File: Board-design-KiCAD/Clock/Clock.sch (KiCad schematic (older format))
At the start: 19 parts, among them M1 SevSeg4Inch, M2 SevSeg4Inch, Y1 SevSeg1.8Inch, Y2 SevSeg1.8Inch, Y3 SevSeg1.8Inch, Y4 SevSeg1.8Inch

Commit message: Add some components
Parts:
- removed U? (x4): ULN2003A, symbol Transistor_Array:ULN2003A
- added U? (x3): 74HC595, symbol 74xx:74HC595
- added U? (x2): ULN2003A, symbol Transistor_Array:ULN2003A
- added U? (x7): 74HC14, symbol 74xx:74HC14
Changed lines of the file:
@@
-$EndComp
-$Comp
-L Transistor_Array:ULN2003A U?
-U 1 1 5F3B85A2
-P 4450 3800
-F 0 "U?" H 4450 4467 50  0000 C CNN
-F 1 "ULN2003A" H 4450 4376 50  0000 C CNN
-F 2 "" H 4500 3250 50  0001 L CNN
-F 3 "http://www.ti.com/lit/ds/symlink/uln2003a.pdf" H 4550 3600 50  0001 C CNN
-	1    4450 3800
-	1    0    0    -1
-$EndComp
-$Comp
-L Transistor_Array:ULN2003A U?
-U 1 1 5F3B9616
-P 5550 3750
-F 0 "U?" H 5550 4417 50  0000 C CNN
-F 1 "ULN2003A" H 5550 4326 50  0000 C CNN
-F 2 "" H 5600 3200 50  0001 L CNN
-F 3 "http://www.ti.com/lit/ds/symlink/uln2003a.pdf" H 5650 3550 50  0001 C CNN
-	1    5550 3750
-	1    0    0    -1
-$EndComp
-$Comp
-L Transistor_Array:ULN2003A U?
-U 1 1 5F3BAC84
-P 6750 3750
-F 0 "U?" H 6750 4417 50  0000 C CNN
-F 1 "ULN2003A" H 6750 4326 50  0000 C CNN
-F 2 "" H 6800 3200 50  0001 L CNN
-F 3 "http://www.ti.com/lit/ds/symlink/uln2003a.pdf" H 6850 3550 50  0001 C CNN
-	1    6750 3750
-	1    0    0    -1
-$EndComp
-$Comp
-L Transistor_Array:ULN2003A U?
-U 1 1 5F3BBFEA
-P 7950 3700
-F 0 "U?" H 7950 4367 50  0000 C CNN
-F 1 "ULN2003A" H 7950 4276 50  0000 C CNN
-F 2 "" H 8000 3150 50  0001 L CNN
-F 3 "http://www.ti.com/lit/ds/symlink/uln2003a.pdf" H 8050 3500 50  0001 C CNN
-	1    7950 3700
-	1    0    0    -1
 $EndComp
 $Comp
@@
 	1    0    0    -1
 $EndComp
-$Comp
-L power:GND #PWR?
-U 1 1 5F3CCD46
-P 4450 4550
-F 0 "#PWR?" H 4450 4300 50  0001 C CNN
-F 1 "GND" H 4455 4377 50  0000 C CNN
-F 2 "" H 4450 4550 50  0001 C CNN
-F 3 "" H 4450 4550 50  0001 C CNN
-	1    4450 4550
-	1    0    0    -1
-$EndComp
-$Comp
-L power:GND #PWR?
-U 1 1 5F3CD13E
-P 5550 4550
-F 0 "#PWR?" H 5550 4300 50  0001 C CNN
-F 1 "GND" H 5555 4377 50  0000 C CNN
-F 2 "" H 5550 4550 50  0001 C CNN
-F 3 "" H 5550 4550 50  0001 C CNN
-	1    5550 4550
-	1    0    0    -1
-$EndComp
-$Comp
-L power:GND #PWR?
-U 1 1 5F3CD53D
-P 6750 4500
-F 0 "#PWR?" H 6750 4250 50  0001 C CNN
-F 1 "GND" H 6755 4327 50  0000 C CNN
-F 2 "" H 6750 4500 50  0001 C CNN
-F 3 "" H 6750 4500 50  0001 C CNN
-	1    6750 4500
-	1    0    0    -1
-$EndComp
-$Comp
-L power:GND #PWR?
-U 1 1 5F3CD948
-P 7950 4400
-F 0 "#PWR?" H 7950 4150 50  0001 C CNN
-F 1 "GND" H 7955 4227 50  0000 C CNN
-F 2 "" H 7950 4400 50  0001 C CNN
-F 3 "" H 7950 4400 50  0001 C CNN
-	1    7950 4400
-	1    0    0    -1
-$EndComp
 Wire Wire Line
 	2000 4450 2000 4550
 Wire Wire Line
 	3300 4400 3300 4550
-Wire Wire Line
-	4450 4400 4450 4550
-Wire Wire Line
-	5550 4350 5550 4550
-Wire Wire Line
-	6750 4350 6750 4500
-Wire Wire Line
-	7950 4300 7950 4400
 $Comp
 L Custom:SevSeg1.8Inch Y3
@@
 	1    0    0    -1
 $EndComp
+$Comp
+L 74xx:74HC595 U?
+U 1 1 5F61C67C
+P 4800 3750
+F 0 "U?" H 4800 4531 50  0000 C CNN
+F 1 "74HC595" H 4800 4440 50  0000 C CNN
+F 2 "" H 4800 3750 50  0001 C CNN
+F 3 "http://www.ti.com/lit/ds/symlink/sn74hc595.pdf" H 4800 3750 50  0001 C CNN
+	1    4800 3750
+	1    0    0    -1
+$EndComp
+$Comp
+L 74xx:74HC595 U?
+U 1 1 5F61CF1D
+P 6150 3750
+F 0 "U?" H 6150 4531 50  0000 C CNN
+F 1 "74HC595" H 6150 4440 50  0000 C CNN
+F 2 "" H 6150 3750 50  0001 C CNN
+F 3 "http://www.ti.com/lit/ds/symlink/sn74hc595.pdf" H 6150 3750 50  0001 C CNN
+	1    6150 3750
+	1    0    0    -1
+$EndComp
+$Comp
+L 74xx:74HC595 U?
+U 1 1 5F61DB6E
+P 7550 3750
+F 0 "U?" H 7550 4531 50  0000 C CNN
+F 1 "74HC595" H 7550 4440 50  0000 C CNN
+F 2 "" H 7550 3750 50  0001 C CNN
+F 3 "http://www.ti.com/lit/ds/symlink/sn74hc595.pdf" H 7550 3750 50  0001 C CNN
+	1    7550 3750
+	1    0    0    -1
+$EndComp
+$Comp
+L Transistor_Array:ULN2003A U?
+U 1 1 5F61F098
+P 8450 1700
+F 0 "U?" H 8450 2367 50  0000 C CNN
+F 1 "ULN2003A" H 8450 2276 50  0000 C CNN
+F 2 "" H 8500 1150 50  0001 L CNN
+F 3 "http://www.ti.com/lit/ds/symlink/uln2003a.pdf" H 8550 1500 50  0001 C CNN
+	1    8450 1700
+	1    0    0    -1
+$EndComp
+$Comp
+L Transistor_Array:ULN2003A U?
+U 1 1 5F6203B3
+P 9750 1700
+F 0 "U?" H 9750 2367 50  0000 C CNN
+F 1 "ULN2003A" H 9750 2276 50  0000 C CNN
+F 2 "" H 9800 1150 50  0001 L CNN
+F 3 "http://www.ti.com/lit/ds/symlink/uln2003a.pdf" H 9850 1500 50  0001 C CNN
+	1    9750 1700
+	1    0    0    -1
+$EndComp
+$Comp
+L 74xx:74HC14 U?
+U 1 1 5F621AF3
+P 9150 3250
+F 0 "U?" H 9150 3567 50  0000 C CNN
+F 1 "74HC14" H 9150 3476 50  0000 C CNN
+F 2 "" H 9150 3250 50  0001 C CNN
+F 3 "http://www.ti.com/lit/gpn/sn74HC14" H 9150 3250 50  0001 C CNN
+	1    9150 3250
+	1    0    0    -1
+$EndComp
+$Comp
+L 74xx:74HC14 U?
+U 2 1 5F623073
+P 9150 3700
+F 0 "U?" H 9150 4017 50  0000 C CNN
+F 1 "74HC14" H 9150 3926 50  0000 C CNN
+F 2 "" H 9150 3700 50  0001 C CNN
+F 3 "http://www.ti.com/lit/gpn/sn74HC14" H 9150 3700 50  0001 C CNN
+	2    9150 3700
+	1    0    0    -1
+$EndComp
+$Comp
+L 74xx:74HC14 U?
+U 3 1 5F62444F
+P 9150 4100
+F 0 "U?" H 9150 4417 50  0000 C CNN
+F 1 "74HC14" H 9150 4326 50  0000 C CNN
+F 2 "" H 9150 4100 50  0001 C CNN
+F 3 "http://www.ti.com/lit/gpn/sn74HC14" H 9150 4100 50  0001 C CNN
+	3    9150 4100
+	1    0    0    -1
+$EndComp
+$Comp
+L 74xx:74HC14 U?
+U 4 1 5F62485C
+P 9150 4600
+F 0 "U?" H 9150 4917 50  0000 C CNN
+F 1 "74HC14" H 9150 4826 50  0000 C CNN
+F 2 "" H 9150 4600 50  0001 C CNN
+F 3 "http://www.ti.com/lit/gpn/sn74HC14" H 9150 4600 50  0001 C CNN
+	4    9150 4600
+	1    0    0    -1
+$EndComp
+$Comp
+L 74xx:74HC14 U?
+U 5 1 5F625C4A
+P 9150 5050
+F 0 "U?" H 9150 5367 50  0000 C CNN
+F 1 "74HC14" H 9150 5276 50  0000 C CNN
+F 2 "" H 9150 5050 50  0001 C CNN
+F 3 "http://www.ti.com/lit/gpn/sn74HC14" H 9150 5050 50  0001 C CNN
+	5    9150 5050
+	1    0    0    -1
+$EndComp
+$Comp
+L 74xx:74HC14 U?
+U 6 1 5F627579
+P 9150 5450
+F 0 "U?" H 9150 5767 50  0000 C CNN
+F 1 "74HC14" H 9150 5676 50  0000 C CNN
+F 2 "" H 9150 5450 50  0001 C CNN
+F 3 "http://www.ti.com/lit/gpn/sn74HC14" H 9150 5450 50  0001 C CNN
+	6    9150 5450
+	1    0    0    -1
+$EndComp
+$Comp
+L 74xx:74HC14 U?
+U 7 1 5F62877C
+P 8100 5450
+F 0 "U?" H 8330 5496 50  0000 L CNN
+F 1 "74HC14" H 8330 5405 50  0000 L CNN
+F 2 "" H 8100 5450 50  0001 C CNN
+F 3 "http://www.ti.com/lit/gpn/sn74HC14" H 8100 5450 50  0001 C CNN
+	7    8100 5450
+	1    0    0    -1
+$EndComp

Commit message: Add power supply and 11-V regulator
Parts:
- removed U? (x7): 74HC14, symbol 74xx:74HC14
- added Cff: C, symbol Device:C
- added Cin, Cout: CP1, symbol Device:CP1
- added D1: D_Schottky, symbol Device:D_Schottky
- added L1: L, symbol Device:L
- added PowerSupply: Barrel_Jack_Switch, symbol Connector:Barrel_Jack_Switch
- added R1, R2: R_US, symbol Device:R_US
- added R_CONTROL: R_POT_US, symbol Device:R_POT_US
- added Regulator-11V: LM2596T-ADJ, Package_TO_SOT_THT:TO-220-5_P3.4x3.7mm_StaggerOdd_Lead3.8mm_Vertical, symbol Regulator_Switching:LM2596T-ADJ
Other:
- moved on the sheet: D1, D2, H1, H2, M1, M2, Mo1, Mo2, U?, Y1, Y2, Y3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

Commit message: Nada
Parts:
- PowerSupply: footprint (none) -> Connector_BarrelJack:BarrelJack_Horizontal
- Regulator-11V: footprint Package_TO_SOT_THT:TO-220-5_P3.4x3.7mm_StaggerOdd_Lead3.8mm_Vertical -> Package_TO_SOT_THT:TO-220-5_Horizontal_TabUp
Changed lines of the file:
@@
 U 1 1 5F648FD6
 P 2300 1250
-F 0 "Regulator-11V" H 2300 1617 50  0000 C CNN
-F 1 "LM2596T-ADJ" H 2300 1526 50  0000 C CNN
-F 2 "Package_TO_SOT_THT:TO-220-5_P3.4x3.7mm_StaggerOdd_Lead3.8mm_Vertical" H 2350 1000 50  0001 L CIN
+F 0 "Regulator-11V" H 2300 1707 50  0000 C CNN
+F 1 "LM2596T-ADJ" H 2300 1616 50  0000 C CNN
+F 2 "Package_TO_SOT_THT:TO-220-5_Horizontal_TabUp" H 2300 1525 50  0000 C CIN
 F 3 "http://www.ti.com/lit/ds/symlink/lm2596.pdf" H 2300 1250 50  0001 C CNN
 	1    2300 1250
@@
 U 1 1 5F641846
 P 800 1250
-F 0 "PowerSupply" H 857 1567 50  0000 C CNN
-F 1 "Barrel_Jack_Switch" H 857 1476 50  0000 C CNN
-F 2 "" H 850 1210 50  0001 C CNN
+F 0 "PowerSupply" H 857 1657 50  0000 C CNN
+F 1 "Barrel_Jack_Switch" H 857 1566 50  0000 C CNN
+F 2 "Connector_BarrelJack:BarrelJack_Horizontal" H 857 1475 50  0000 C CNN
 F 3 "~" H 850 1210 50  0001 C CNN
 	1    800  1250

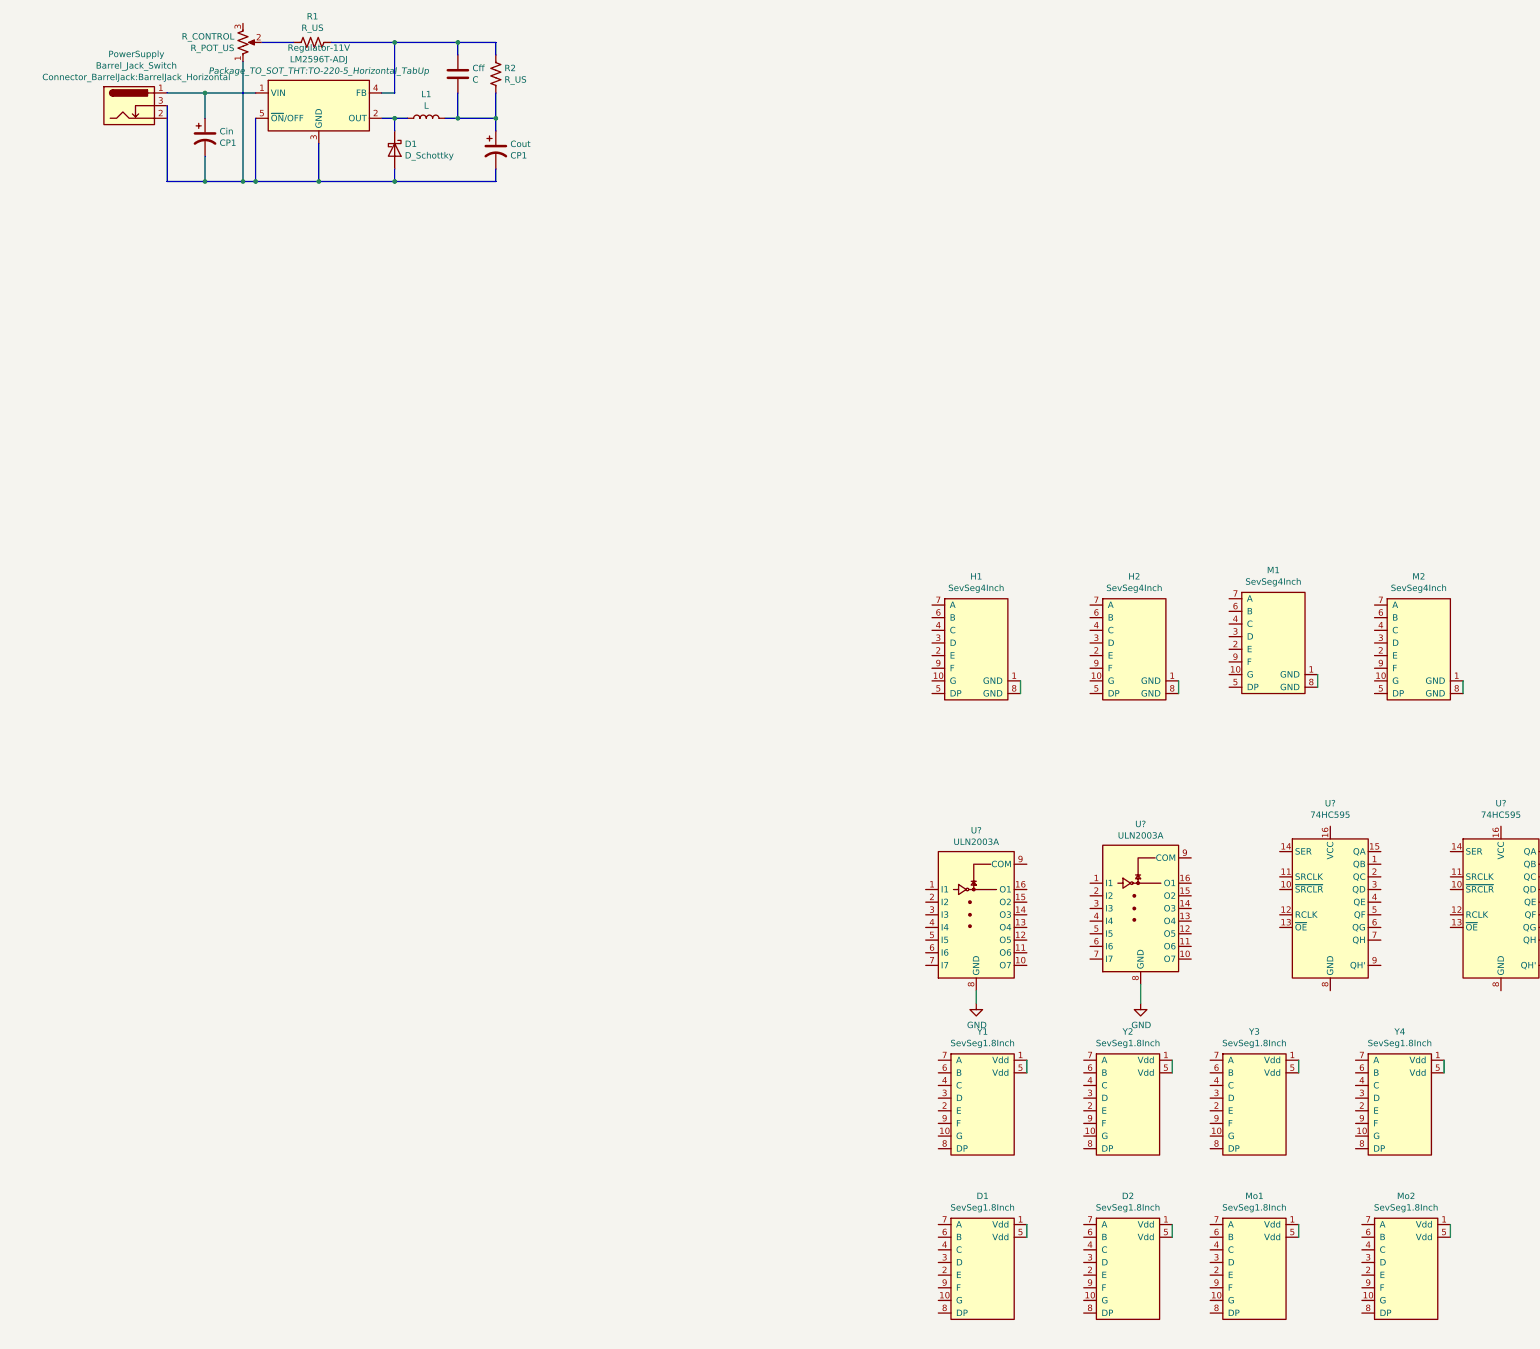
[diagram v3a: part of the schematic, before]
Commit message: Build PCB part for external power supply
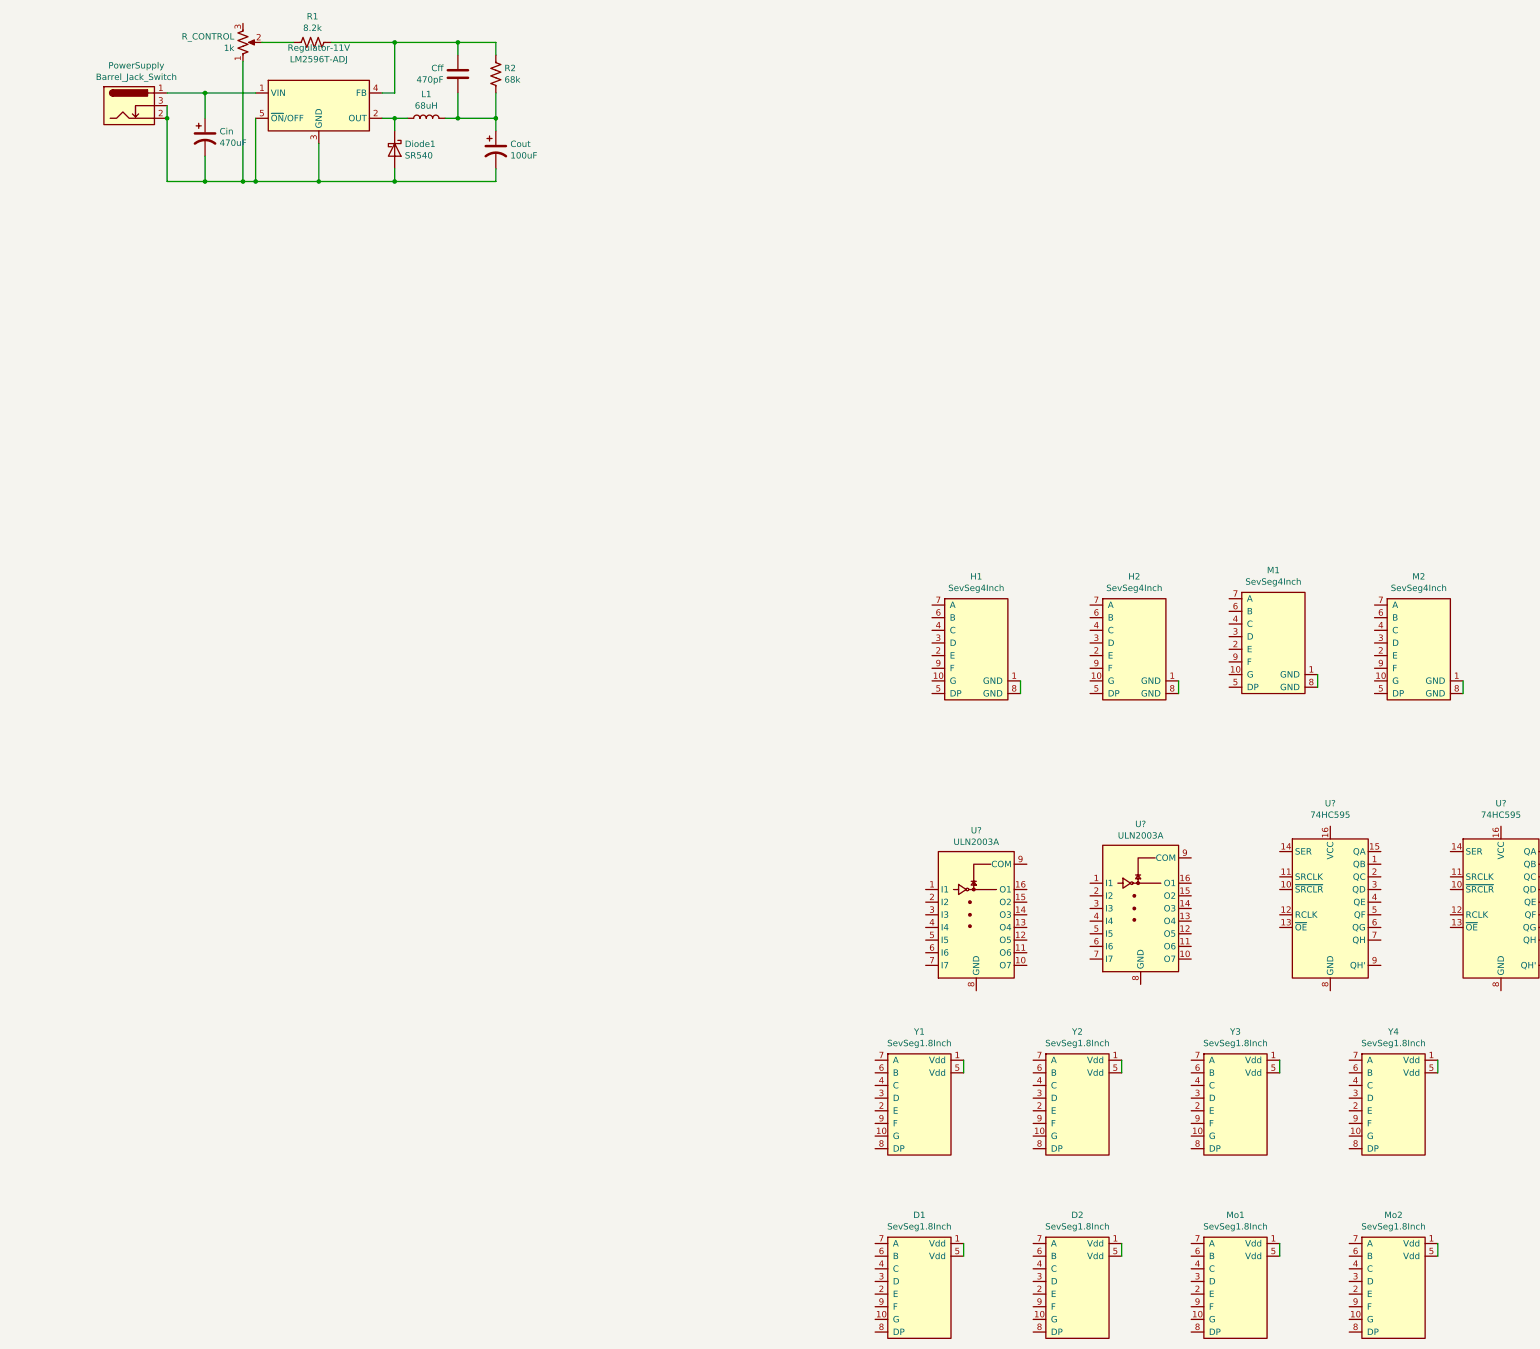
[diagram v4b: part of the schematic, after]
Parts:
- Cff: value C -> 470pF; footprint (none) -> Custom:CP_Radial_H15.0mm_W14.0mm_T8.0mm_P8.5mm_Horizontal
- Cin: value CP1 -> 470uF; footprint (none) -> Capacitor_THT:CP_Radial_D10.0mm_P5.00mm
- Cout: value CP1 -> 100uF; footprint (none) -> Capacitor_THT:CP_Radial_D8.0mm_P3.50mm
- Diode1: renamed from D1; value D_Schottky -> SR540; footprint (none) -> Custom:D_5600_9500Metric
- L1: value L -> 68uH; footprint (none) -> Custom:L_Radial_D10.0mm_P5.5mm
- R1: value R_US -> 8.2k; footprint (none) -> Resistor_THT:R_Axial_DIN0207_L6.3mm_D2.5mm_P10.16mm_Horizontal
- R2: value R_US -> 68k; footprint (none) -> Resistor_THT:R_Axial_DIN0207_L6.3mm_D2.5mm_P10.16mm_Horizontal
- R_CONTROL: value R_POT_US -> 1k; footprint (none) -> Potentiometer_THT:Potentiometer_Vishay_T73YP_Vertical
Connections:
- net at PowerSupply.1: now also Cin.1, Regulator-11V.1 (VIN)
- net at PowerSupply.2: now also Cin.2, Cout.2, Diode1.2 (A), PowerSupply.3, R_CONTROL.1, Regulator-11V.3 (GND), Regulator-11V.5 (~ON~/OFF)
- net at Cout.1: now also Cff.2, L1.2, R2.2
- net at Regulator-11V.2 (OUT): now also Diode1.1 (K), L1.1
- net at Regulator-11V.4 (FB): now also Cff.1, R1.2, R2.1
- net at R_CONTROL.2: now also R1.1
- net GND: no longer names the net of U?.8 (GND)
- net GND: no longer U?.8 (GND)
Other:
- moved on the sheet: D1, D2, Mo1, Mo2, Y1, Y2, Y3, Y4

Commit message: Add some PCB routes
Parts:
- added BCD-DATE1, BCD-TIME1: 74LS47, Package_DIP:DIP-18_W7.62mm_LongPads, symbol 74xx:74LS47
- BCD-YEAR1, CommonPinControl1, InputPowerConverter1: renamed from U?; footprint (none) -> Package_DIP:DIP-18_W7.62mm_LongPads
- D1, D2, Mo1, Mo2, Y1, Y2, Y3, Y4: footprint (none) -> Custom:SevSeg1.8Inch
- gave numbers to parts that had none: 5
- renumbered Cff to Cff1, Cin to Cin1, Cout to Cout1, PowerSupply to PowerSupply1, R_CONTROL to R_CONTROL1, Regulator-11V to Regulator-11V1
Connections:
- net TIME_G: now reaches H1.10 (G)
- net TIME_G: now also H2.10 (G), InputPowerConverter1.10 (O7), M1.10 (G), M2.10 (G)
- net TIME_E: now reaches H1.2 (E)
- net TIME_E: now also H2.2 (E), InputPowerConverter1.12 (O5), M1.6 (B), M2.2 (E)
- net TIME_D: now reaches H1.3 (D)
- net TIME_D: now also H2.3 (D), InputPowerConverter1.13 (O4), M1.7 (A), M2.3 (D)
- net TIME_C: now reaches H1.4 (C)
- net TIME_C: now also H2.4 (C), InputPowerConverter1.14 (O3), M1.9 (F), M2.4 (C)
- net TIME_B: now reaches H1.6 (B)
- net TIME_B: now also H2.6 (B), InputPowerConverter1.15 (O2), M1.2 (E), M2.6 (B)
- net TIME_A: now reaches H1.7 (A)
- net TIME_A: now also H2.7 (A), InputPowerConverter1.16 (O1), M1.3 (D), M2.7 (A)
- net TIME_F: now reaches H1.9 (F)
- net TIME_F: now also H2.9 (F), InputPowerConverter1.11 (O6), M1.4 (C), M2.9 (F)
- net at BCD-YEAR1.10 (d): now also InputPowerConverter1.4 (I4)
- net at BCD-YEAR1.11 (c): now also InputPowerConverter1.3 (I3)
- net at BCD-YEAR1.12 (b): now also InputPowerConverter1.2 (I2)
- net at BCD-YEAR1.13 (a): now also InputPowerConverter1.1 (I1)
- net at BCD-YEAR1.14 (g): now also InputPowerConverter1.7 (I7)
- net at BCD-YEAR1.15 (f): now also InputPowerConverter1.6 (I6)
- net GND: now reaches BCD-YEAR1.8 (GND)
- net GND: now also Cin1.2, CommonPinControl1.8 (GND), Cout1.2, Diode1.2 (A), InputPowerConverter1.8 (GND), PowerSupply1.2, PowerSupply1.3, R_CONTROL1.1, Regulator-11V1.3 (GND), Regulator-11V1.5 (~ON~/OFF)
- net at BCD-YEAR1.9 (e): now also InputPowerConverter1.5 (I5)
- net +11V: now reaches InputPowerConverter1.9 (COM)
- net +11V: now also Cff1.2, CommonPinControl1.9 (COM), Cout1.1, L1.2, R2.2
- net +15V: now reaches Cin1.1, PowerSupply1.1, Regulator-11V1.1 (VIN)
- net OUT: now reaches Diode1.1 (K), L1.1, Regulator-11V1.2 (OUT)
- net FEEDBACK: now reaches Cff1.1, R1.2, R2.1, Regulator-11V1.4 (FB)
- no-connect marks 0 -> 11
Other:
- moved on the sheet: BCD-YEAR1, CommonPinControl1, D1, D2, H1, H2, InputPowerConverter1, M1, M2, Mo1, Mo2, U1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
